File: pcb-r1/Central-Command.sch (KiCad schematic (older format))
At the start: 12 parts, among them P101 CONN_01X10, P102 CONN_01X10, P103 CONN_01X04, P104 CONN_01X02, P105 CONN_01X04, P106 CONN_01X02, U101 STM32F030C8, Y101 Crystal

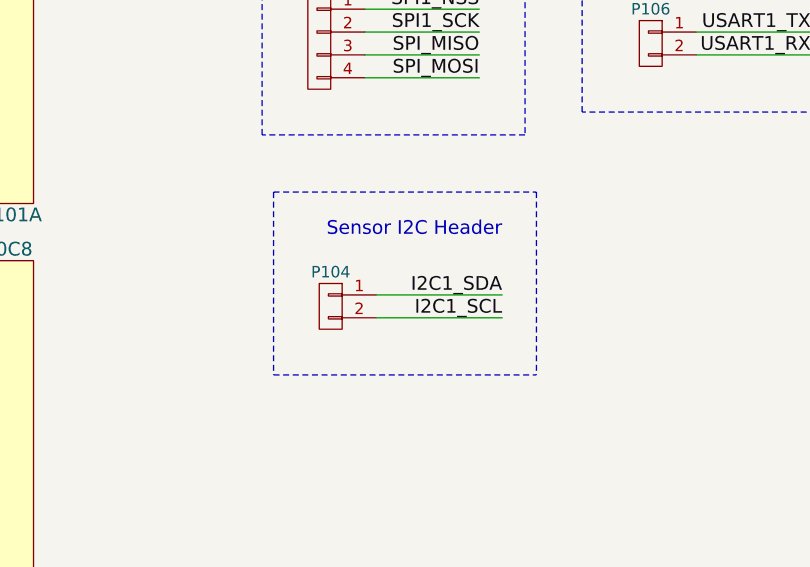
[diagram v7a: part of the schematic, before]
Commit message: Started the part to footprint association
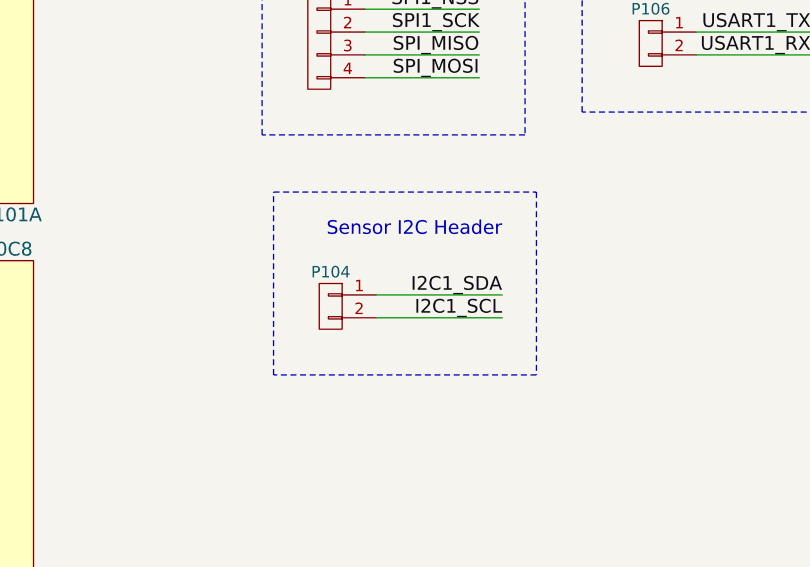
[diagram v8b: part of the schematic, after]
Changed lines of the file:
@@
 $EndComp
 $Comp
-L GND #PWR101
+L GND #PWR01
 U 1 1 5636B68F
 P 2800 3300
-F 0 "#PWR101" H 2800 3050 50  0001 C CNN
+F 0 "#PWR01" H 2800 3050 50  0001 C CNN
 F 1 "GND" H 2800 3150 50  0000 C CNN
 F 2 "" H 2800 3300 60  0000 C CNN
@@
 F 0 "Y101" H 4650 1900 50  0000 C CNN
 F 1 "Crystal" H 4650 1600 50  0000 C CNN
-F 2 "" H 4650 1750 60  0000 C CNN
+F 2 "" H 4650 1750 60  0001 C CNN
 F 3 "" H 4650 1750 60  0000 C CNN
 F 4 "http://parts.io/detail/343558/FOXSLF%2F080-20" H 4650 1750 60  0001 C CNN "Link"
@@
 F 0 "C103" V 5400 2000 50  0000 L CNN
 F 1 "20pF" V 5100 2000 50  0000 L CNN
-F 2 "" H 5288 1850 30  0000 C CNN
+F 2 "" H 5288 1850 30  0001 C CNN
 F 3 "" H 5250 2000 60  0000 C CNN
 	1    5250 2000
@@
 F 0 "C102" V 5400 1550 50  0000 L CNN
 F 1 "20pF" V 5100 1550 50  0000 L CNN
-F 2 "" H 5288 1400 30  0000 C CNN
+F 2 "" H 5288 1400 30  0001 C CNN
 F 3 "" H 5250 1550 60  0000 C CNN
 	1    5250 1550
@@
 $EndComp
 $Comp
-L GND #PWR102
+L GND #PWR02
 U 1 1 5654AC7D
 P 5600 2200
-F 0 "#PWR102" H 5600 1950 50  0001 C CNN
+F 0 "#PWR02" H 5600 1950 50  0001 C CNN
 F 1 "GND" H 5600 2050 50  0000 C CNN
 F 2 "" H 5600 2200 60  0000 C CNN
@@
 F 0 "P101" H 700 5650 50  0000 C CNN
 F 1 "CONN_01X10" V 800 5100 50  0001 C CNN
-F 2 "" H 700 5100 60  0000 C CNN
+F 2 "" H 700 5100 60  0001 C CNN
 F 3 "" H 700 5100 60  0000 C CNN
 	1    700  5100
@@
 F 0 "P102" H 850 2700 50  0000 C CNN
 F 1 "CONN_01X10" V 950 2150 50  0001 C CNN
-F 2 "" H 850 2150 60  0000 C CNN
+F 2 "" H 850 2150 60  0001 C CNN
 F 3 "" H 850 2150 60  0000 C CNN
 	1    850  2150
@@
 F 0 "P105" H 5200 3500 50  0000 C CNN
 F 1 "CONN_01X04" V 5300 3250 50  0001 C CNN
-F 2 "" H 5200 3250 60  0000 C CNN
+F 2 "" H 5200 3250 60  0001 C CNN
 F 3 "" H 5200 3250 60  0000 C CNN
 	1    5200 3250
@@
 $EndComp
 $Comp
-L GND #PWR103
+L GND #PWR03
 U 1 1 5667E90C
 P 5600 3650
-F 0 "#PWR103" H 5600 3400 50  0001 C CNN
+F 0 "#PWR03" H 5600 3400 50  0001 C CNN
 F 1 "GND" H 5600 3500 50  0000 C CNN
 F 2 "" H 5600 3650 60  0000 C CNN
@@
 F 0 "P103" H 4950 4950 50  0000 C CNN
 F 1 "CONN_01X04" V 5050 4700 50  0001 C CNN
-F 2 "" H 4950 4700 60  0000 C CNN
+F 2 "" H 4950 4700 60  0001 C CNN
 F 3 "" H 4950 4700 60  0000 C CNN
 	1    4950 4700
@@
 F 0 "P106" H 6400 4850 50  0000 C CNN
 F 1 "CONN_01X02" V 6500 4700 50  0001 C CNN
-F 2 "" H 6400 4700 60  0000 C CNN
+F 2 "" H 6400 4700 60  0001 C CNN
 F 3 "" H 6400 4700 60  0000 C CNN
 	1    6400 4700
@@
 F 0 "P104" H 5000 6000 50  0000 C CNN
 F 1 "CONN_01X02" V 5100 5850 50  0001 C CNN
-F 2 "" H 5000 5850 60  0000 C CNN
+F 2 "" H 5000 5850 60  0001 C CNN
 F 3 "" H 5000 5850 60  0000 C CNN
 	1    5000 5850
@@
 	5900 5350 5900 6150
 Wire Notes Line
-	4750 6150 5900 6150
-Wire Notes Line
-	4750 5350 4750 6150
+	5900 6150 4750 6150
+Wire Notes Line
+	4750 6150 4750 5350
 Text Notes 5750 5550 2    60   ~ 0
 Sensor I2C Header
@@
 USART2_RX
 $Comp
-L GND #PWR?
+L GND #PWR04
 U 1 1 56673817
 P 4000 1350
-F 0 "#PWR?" H 4000 1100 50  0001 C CNN
+F 0 "#PWR04" H 4000 1100 50  0001 C CNN
 F 1 "GND" H 4000 1200 50  0000 C CNN
 F 2 "" H 4000 1350 60  0000 C CNN
@@
 	4000 1200 4000 1350
 $Comp
-L GND #PWR?
+L GND #PWR05
 U 1 1 56673B6E
 P 9450 5050
-F 0 "#PWR?" H 9450 4800 50  0001 C CNN
+F 0 "#PWR05" H 9450 4800 50  0001 C CNN
 F 1 "GND" H 9450 4900 50  0000 C CNN
 F 2 "" H 9450 5050 60  0000 C CNN
